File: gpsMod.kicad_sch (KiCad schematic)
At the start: 30 parts, among them U2 MAX2769B, U3 MAX8510EXK29+T, U4 MAX8510EXK29+T, Y1 TXETCDSANF-16.368000

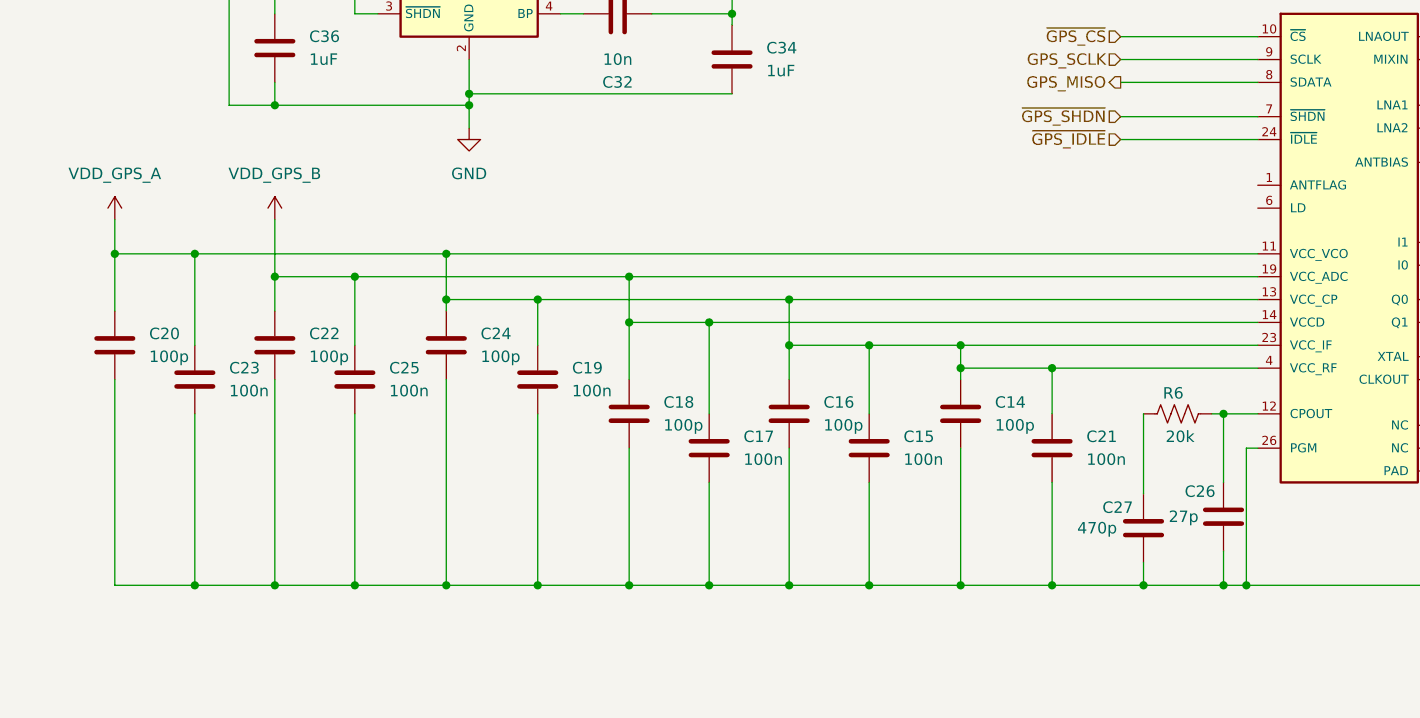
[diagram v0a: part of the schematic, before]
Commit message: Finished schematic.  Time to layout.
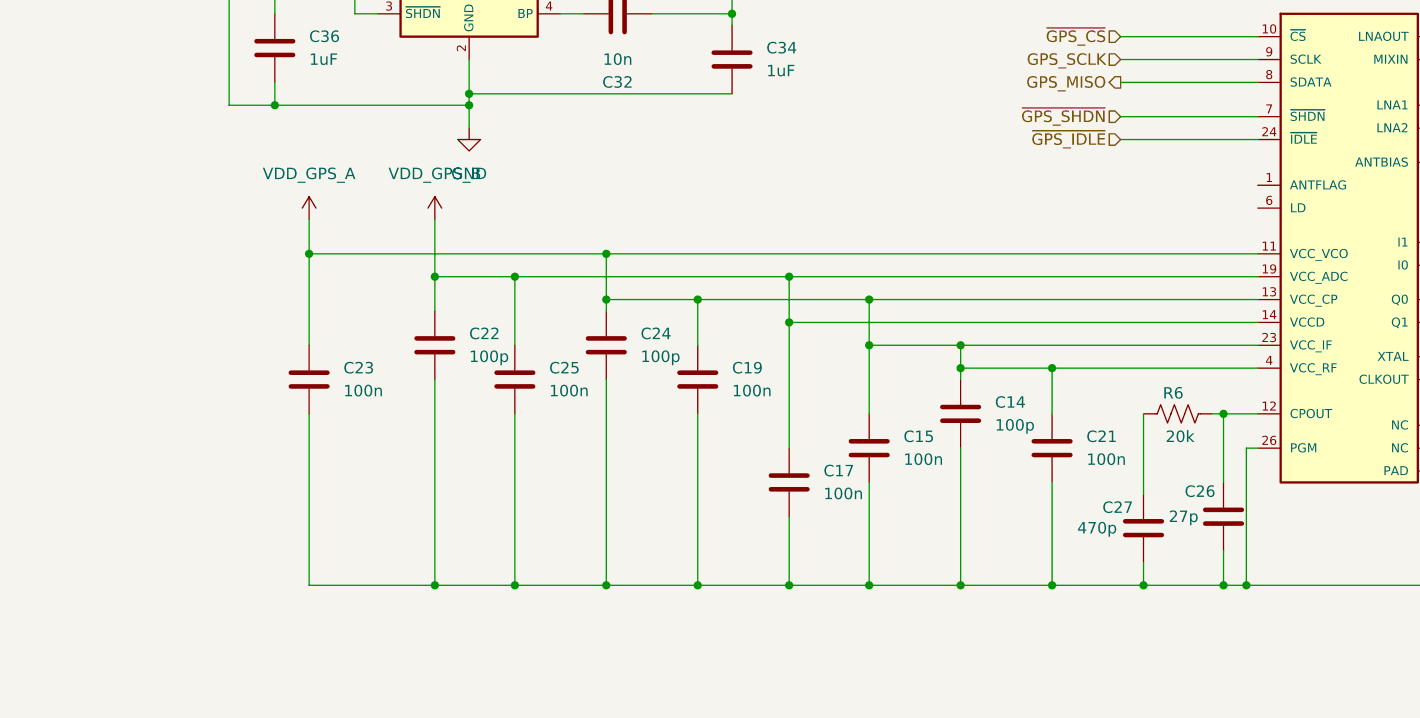
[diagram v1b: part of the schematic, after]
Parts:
- removed C16, C18, C20: 100p, AllardChip:CAPC60X30X33L15L, symbol AllardPassive:C10AB1-10000
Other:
- moved on the sheet: C17, C19, C22, C23, C24, C25

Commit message: Moving parts around to start layout.
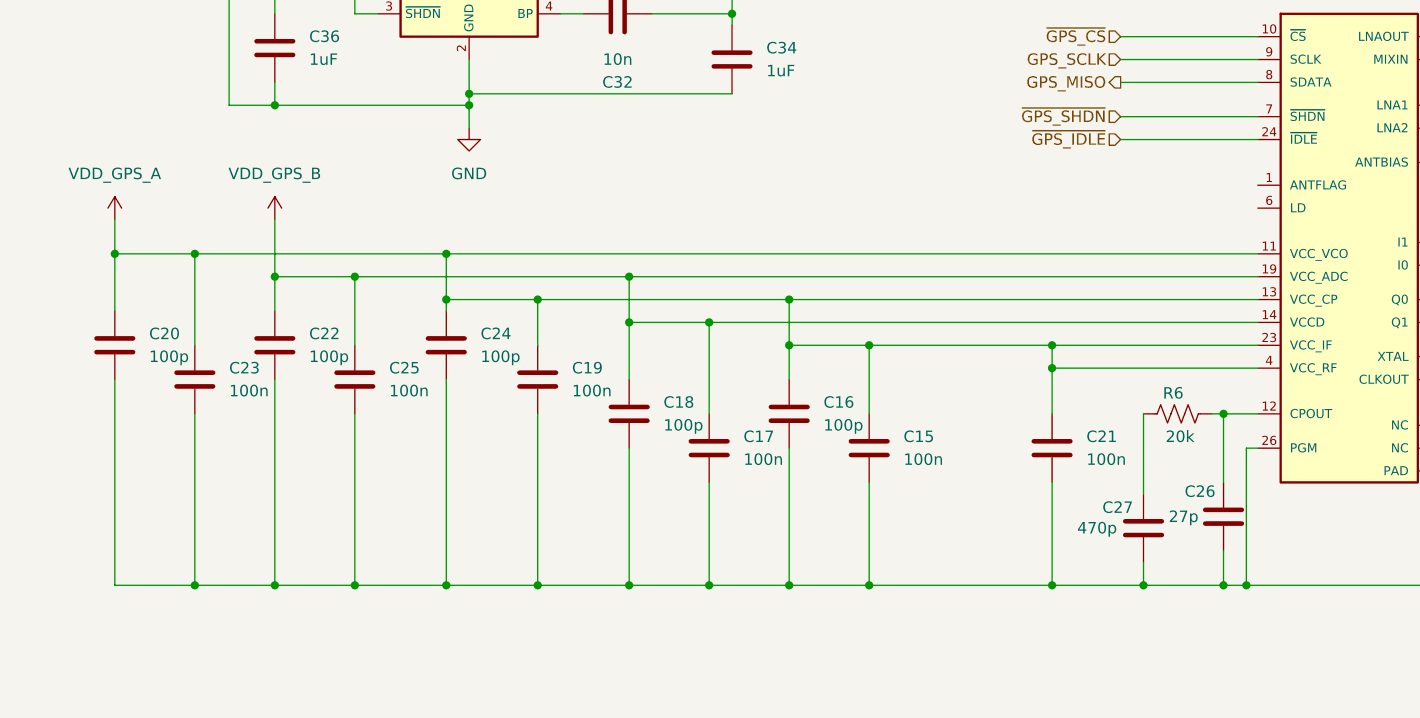
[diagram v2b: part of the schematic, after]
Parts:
- removed C14: 100p, AllardChip:CAPC60X30X33L15L, symbol AllardPassive:C10AB1-10000
- added C16, C18, C20: 100p, AllardChip:CAPC60X30X33L15L, symbol AllardPassive:C10AB1-10000
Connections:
- net GND: now also C16.2, C18.2, C20.2
- net VDD_GPS_A: now also C16.1, C20.1
- net VDD_GPS_B: now also C18.1
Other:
- moved on the sheet: C17, C19, C22, C23, C24, C25

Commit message: starting to lay the board out.
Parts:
- removed C16, C18, C20: 100p, AllardChip:CAPC60X30X33L15L, symbol AllardPassive:C10AB1-10000
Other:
- moved on the sheet: C17, C19, C22, C23, C24, C25
